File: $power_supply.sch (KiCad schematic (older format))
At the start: 26 parts

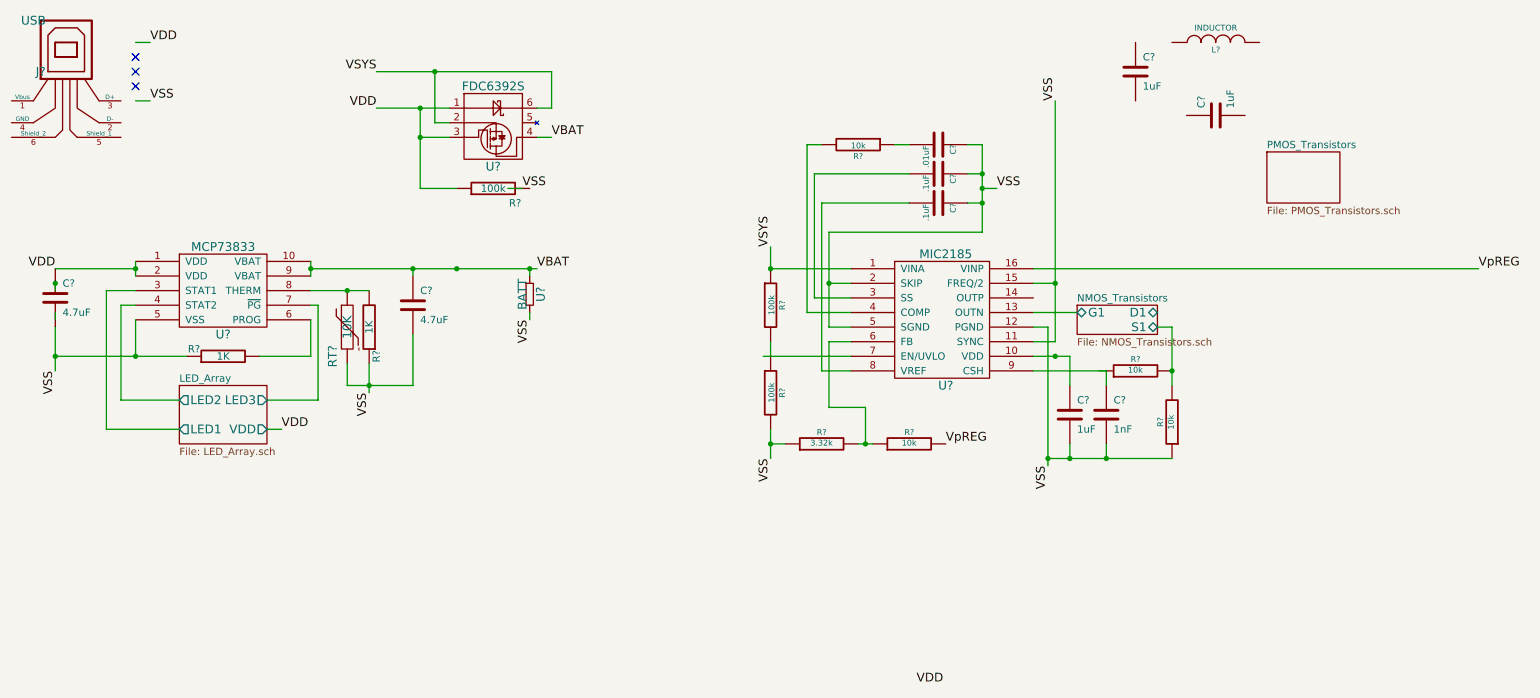
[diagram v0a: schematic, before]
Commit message: Power Supply Schematic
Completed schematic up through the MIC2185

Regulated output voltage named VpREG

Custom components listed in power_supply-cache.lib
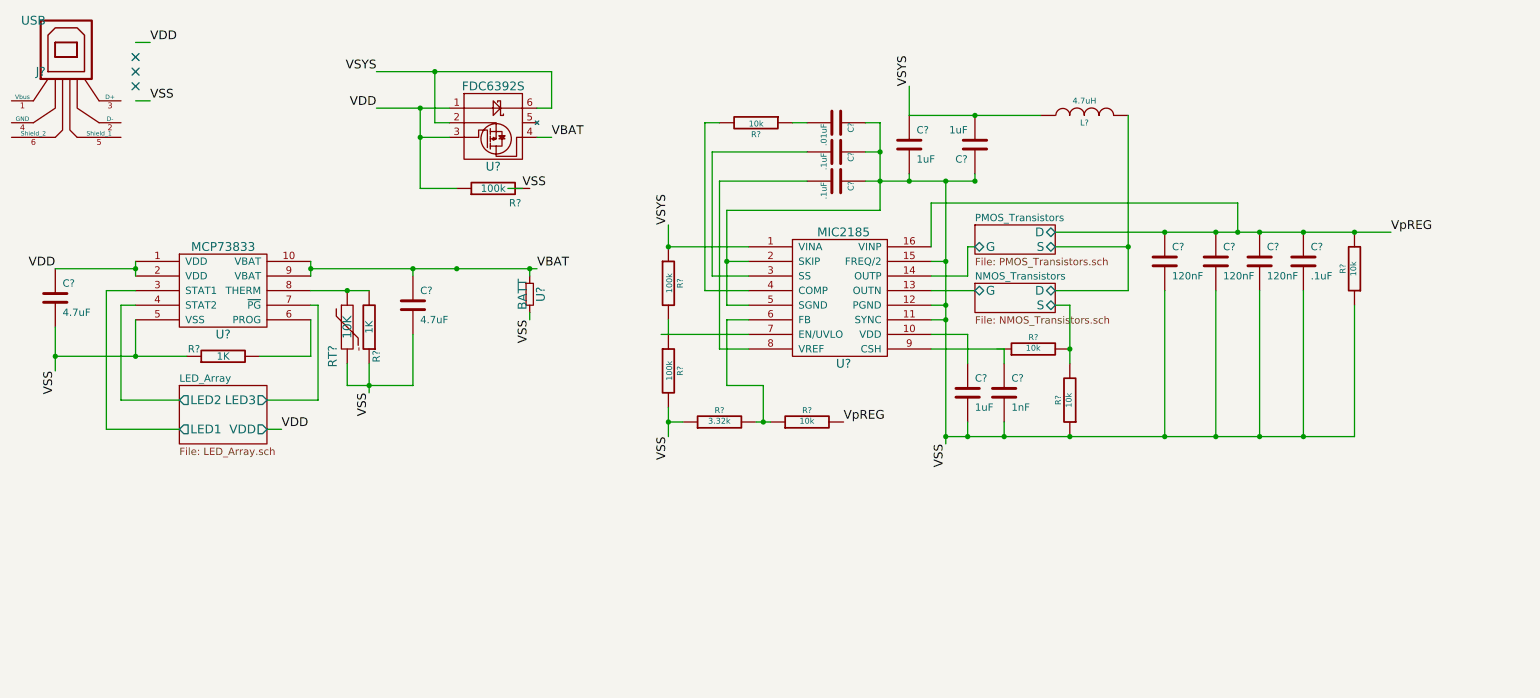
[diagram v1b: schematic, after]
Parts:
- added C? (x3): 120nF, symbol C
- added C?: .1uF, symbol C
- added R?: 10k, ~, symbol R
- L?: value INDUCTOR -> 4.7uH
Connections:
- wire segments 88 -> 102
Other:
- moved on the sheet: C?, L?, R?, U?
